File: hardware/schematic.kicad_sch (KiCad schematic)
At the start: 16 parts, among them M1 Arctic_P12_PRO, U1 DS18B20, U2 TC1602A-01T

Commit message: hw: update schematic
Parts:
- removed U2: TC1602A-01T, Display:LCD-016N002L, symbol Display_Character:LCD-016N002L
- added U2: NHD-0420H1Z, Display:NHD-0420H1Z, symbol Display_Character:NHD-0420H1Z
- added U3: PCF8574, symbol Interface_Expansion:PCF8574
- R1: value 220Ω -> 4.7kΩ
- R5: value 15kΩ -> 10kΩ
- R6: value 220Ω -> 2.2kΩ
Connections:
- net +5V: now also U2.2 (VDD), U3.16 (VDD); no longer R6.2
- net GND: now also R6.2, U2.1 (VSS), U2.10 (DB3), U2.16 (K), U2.3 (VO), U2.7 (DB0), U2.8 (DB1), U2.9 (DB2), U3.1 (A0), U3.2 (A1), U3.3 (A2), U3.8 (VSS); no longer R1.2, R3.2
- net at M1.4 (PWM): now also A1.24 (D9); no longer A1.19 (D4)
- net at R4.1, U1.2 (DQ): now also A1.19 (D4); no longer A1.18 (D3)
- net at R6.1: now also R1.2
- net at R1.1: now also R3.2
- net at R3.1, R5.1: now also A1.18 (D3); no longer A1.20 (D5)
- net at A1.31 (SDA/A4): now also U3.15 (SDA)
- net at A1.32 (SCL/A5): now also U3.14 (SCL)
- new net: U2.11 (DB4), U3.9 (P4)
- new net: U2.12 (DB5), U3.10 (P5)
- new net: U2.13 (DB6), U3.11 (P6)
- new net: U2.14 (DB7), U3.12 (P7)
- new net: U2.15 (A), U3.7 (P3)
- new net: U2.4 (RS), U3.4 (P0)
- new net: U2.5 (R/W), U3.5 (P1)
- new net: U2.6 (E), U3.6 (P2)
- no-connect marks 27 -> 23

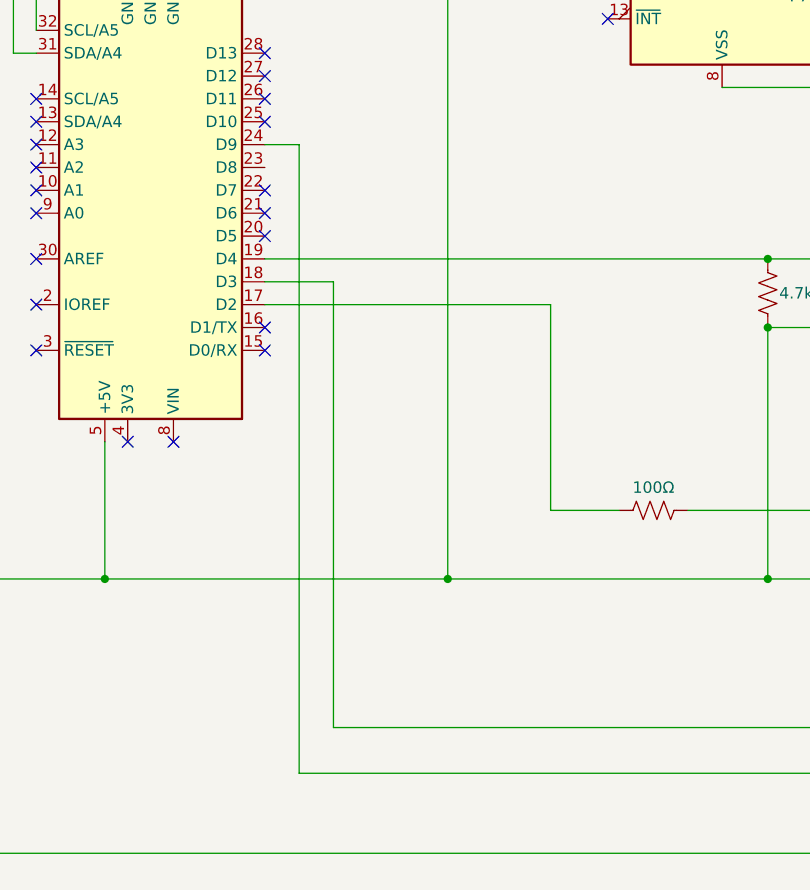
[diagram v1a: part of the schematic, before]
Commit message: hw: update schematic, sw: update pin_definitions.h
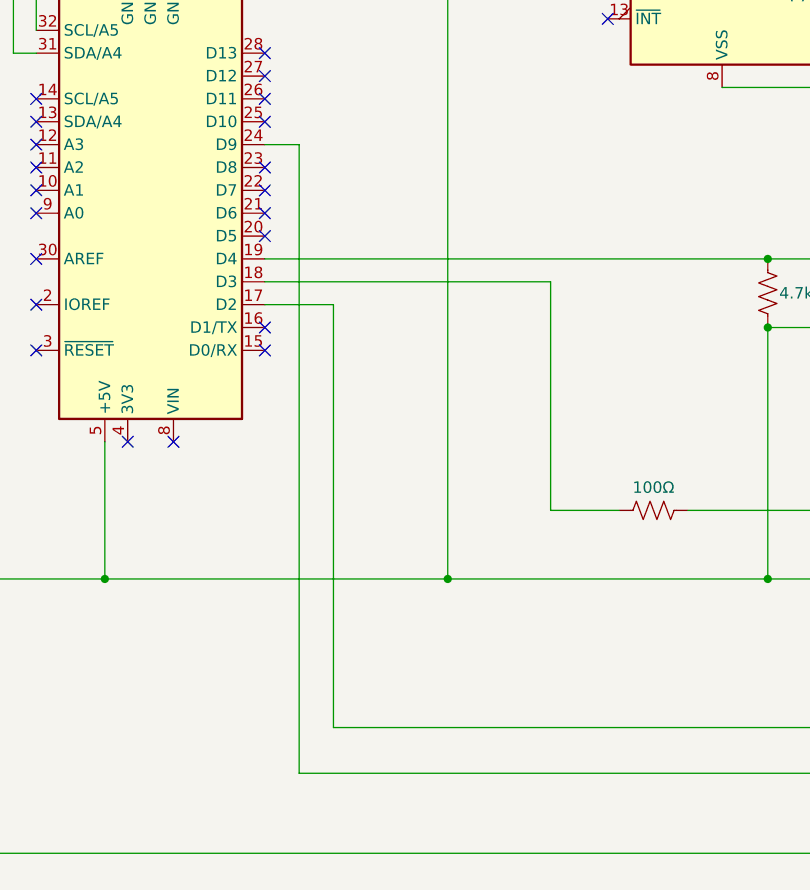
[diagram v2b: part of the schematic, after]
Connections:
- net at R2.1: now also A1.18 (D3); no longer A1.17 (D2)
- net at R3.1, R5.1: now also A1.17 (D2); no longer A1.18 (D3)
- no-connect marks 23 -> 24
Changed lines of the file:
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@@
   (junction (at 45.72 120.65) (diameter 0) (color 0 0 0 0)
   )
+  (no_connect (at 76.2 74.93))
   (no_connect (at 66.04 105.41))
   (no_connect (at 50.8 74.93))
@@
     (stroke (width 0) (type default))
   )
-  (wire (pts (xy 107.95 90.17) (xy 107.95 113.03))
-    (stroke (width 0) (type default))
-  )
   (wire (pts (xy 45.72 44.45) (xy 45.72 120.65))
     (stroke (width 0) (type default))
@@
     (stroke (width 0) (type default))
   )
+  (wire (pts (xy 107.95 113.03) (xy 107.95 87.63))
+    (stroke (width 0) (type default))
+  )
   (wire (pts (xy 109.22 48.26) (xy 109.22 20.32))
     (stroke (width 0) (type default))
@@
     (stroke (width 0) (type default))
   )
+  (wire (pts (xy 83.82 90.17) (xy 76.2 90.17))
+    (stroke (width 0) (type default))
+  )
   (wire (pts (xy 245.11 58.42) (xy 266.7 58.42))
     (stroke (width 0) (type default))
@@
     (stroke (width 0) (type default))
   )
-  (wire (pts (xy 76.2 90.17) (xy 107.95 90.17))
-    (stroke (width 0) (type default))
-  )
   (wire (pts (xy 250.19 142.24) (xy 250.19 144.78))
     (stroke (width 0) (type default))
@@
     (stroke (width 0) (type default))
   )
-  (wire (pts (xy 83.82 87.63) (xy 76.2 87.63))
-    (stroke (width 0) (type default))
-  )
   (wire (pts (xy 267.97 132.08) (xy 250.19 132.08))
     (stroke (width 0) (type default))
@@
     (stroke (width 0) (type default))
   )
+  (wire (pts (xy 107.95 87.63) (xy 76.2 87.63))
+    (stroke (width 0) (type default))
+  )
   (wire (pts (xy 111.76 20.32) (xy 153.67 20.32))
     (stroke (width 0) (type default))
@@
     (stroke (width 0) (type default))
   )
-  (wire (pts (xy 83.82 137.16) (xy 83.82 87.63))
-    (stroke (width 0) (type default))
-  )
   (wire (pts (xy 201.93 55.88) (xy 201.93 68.58))
     (stroke (width 0) (type default))
@@
     (stroke (width 0) (type default))
   )
+  (wire (pts (xy 83.82 137.16) (xy 83.82 90.17))
+    (stroke (width 0) (type default))
+  )

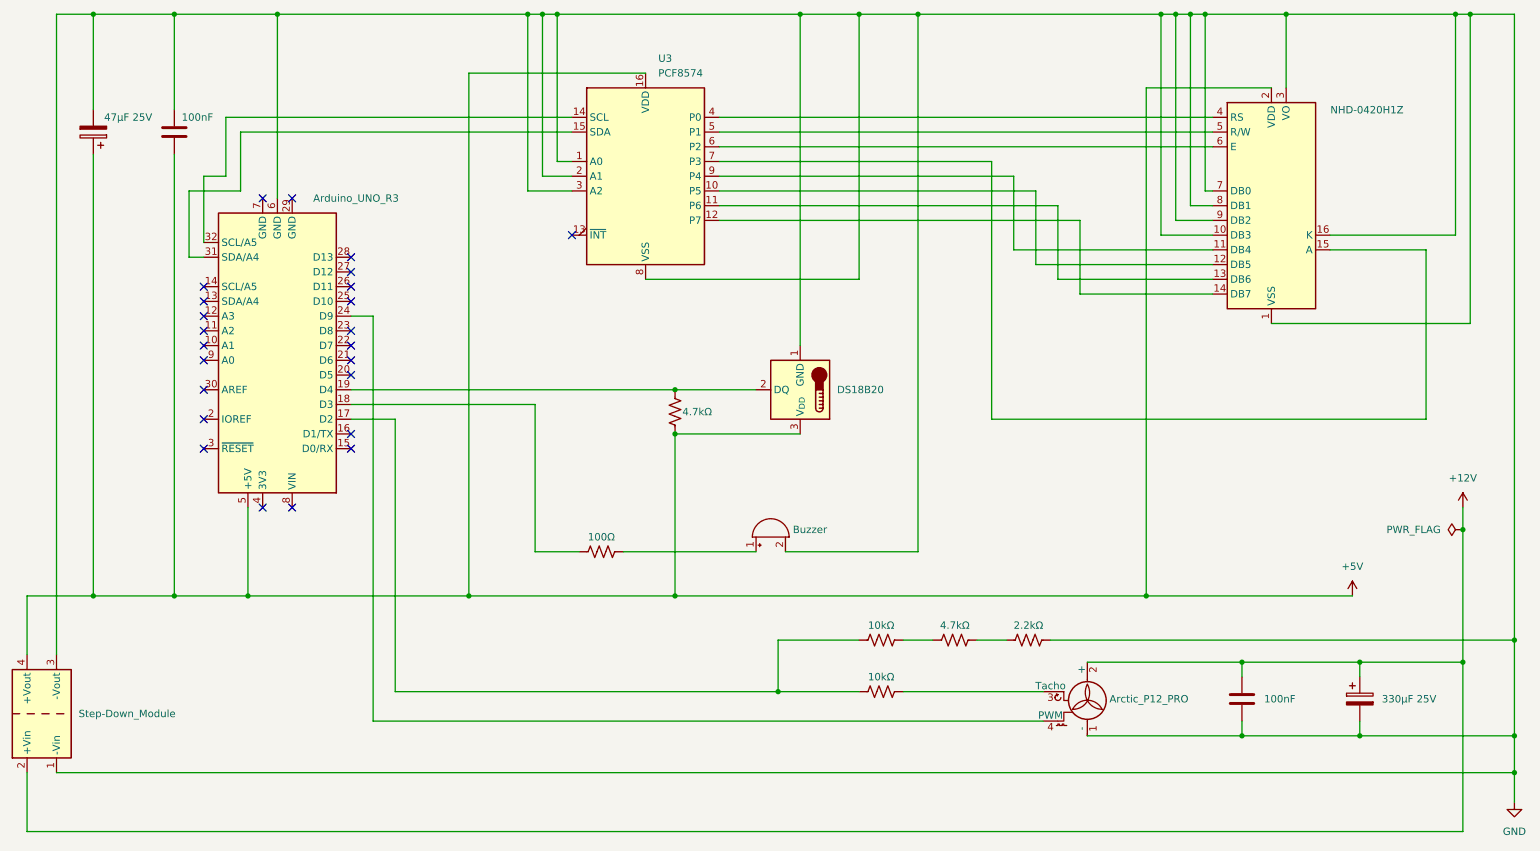
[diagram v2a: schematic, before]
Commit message: add status LEDs to schematic and board configuration
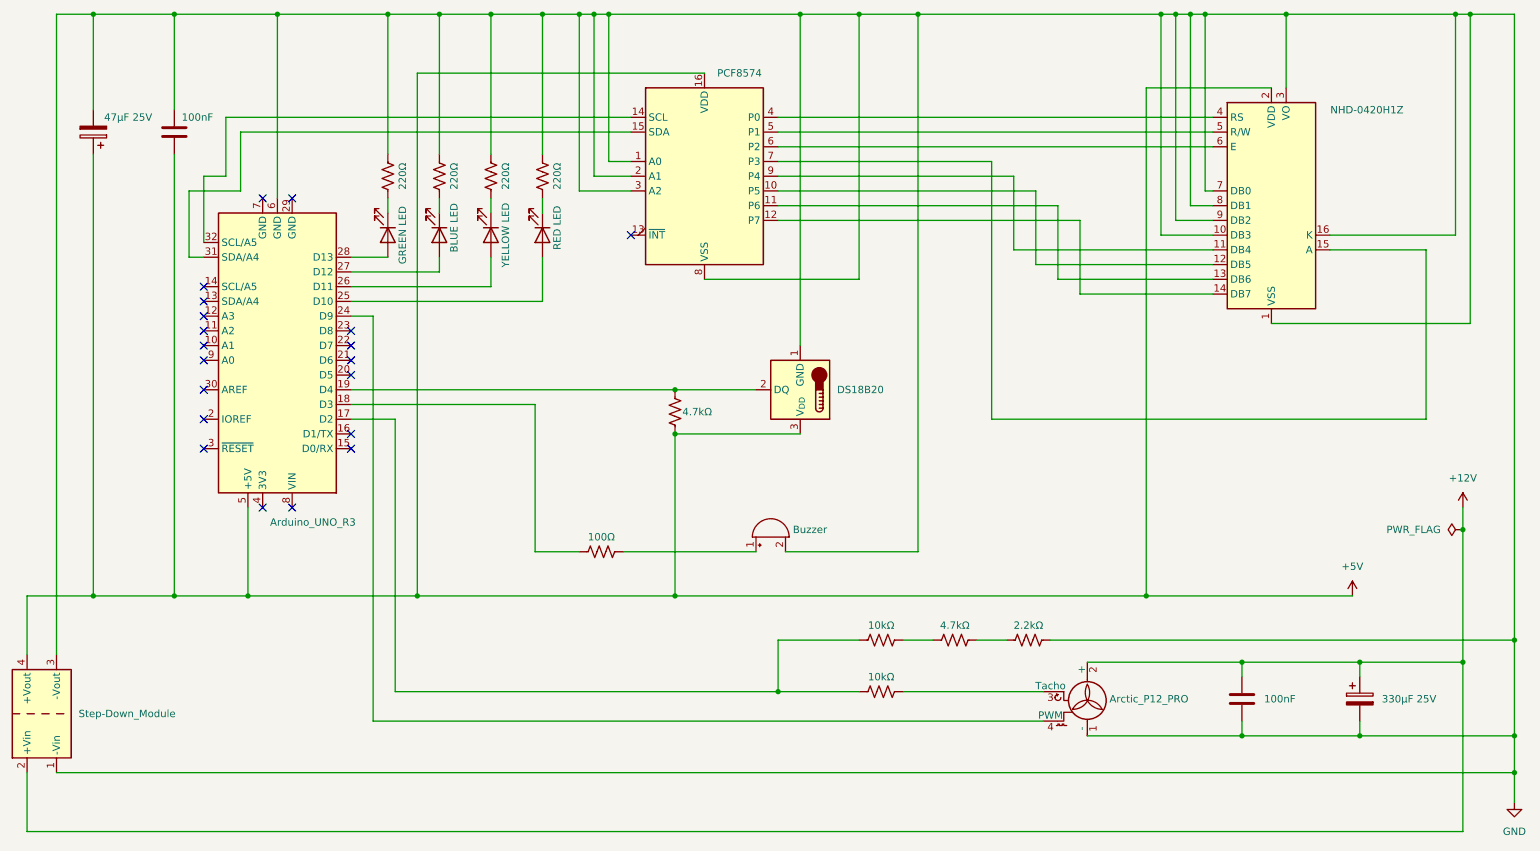
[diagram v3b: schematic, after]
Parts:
- added D1: GREEN LED, symbol Device:LED
- added D2: YELLOW LED, symbol Device:LED
- added D3: BLUE LED, symbol Device:LED
- added D4: RED LED, symbol Device:LED
- added R10, R7, R8, R9: 220Ω, symbol Device:R_US
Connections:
- net GND: now also R10.1, R7.2, R8.2, R9.2
- net at A1.25 (D10): now also D4.2 (A)
- net at A1.26 (D11): now also D2.2 (A)
- net at A1.27 (D12): now also D3.2 (A)
- net at A1.28 (D13): now also D1.2 (A)
- new net: D2.1 (K), R7.1
- new net: D4.1 (K), R8.1
- new net: D1.1 (K), R9.1
- new net: D3.1 (K), R10.2
- no-connect marks 24 -> 20

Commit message: hw: update schematic, sw: update main, config, fan, buzzer, lcd
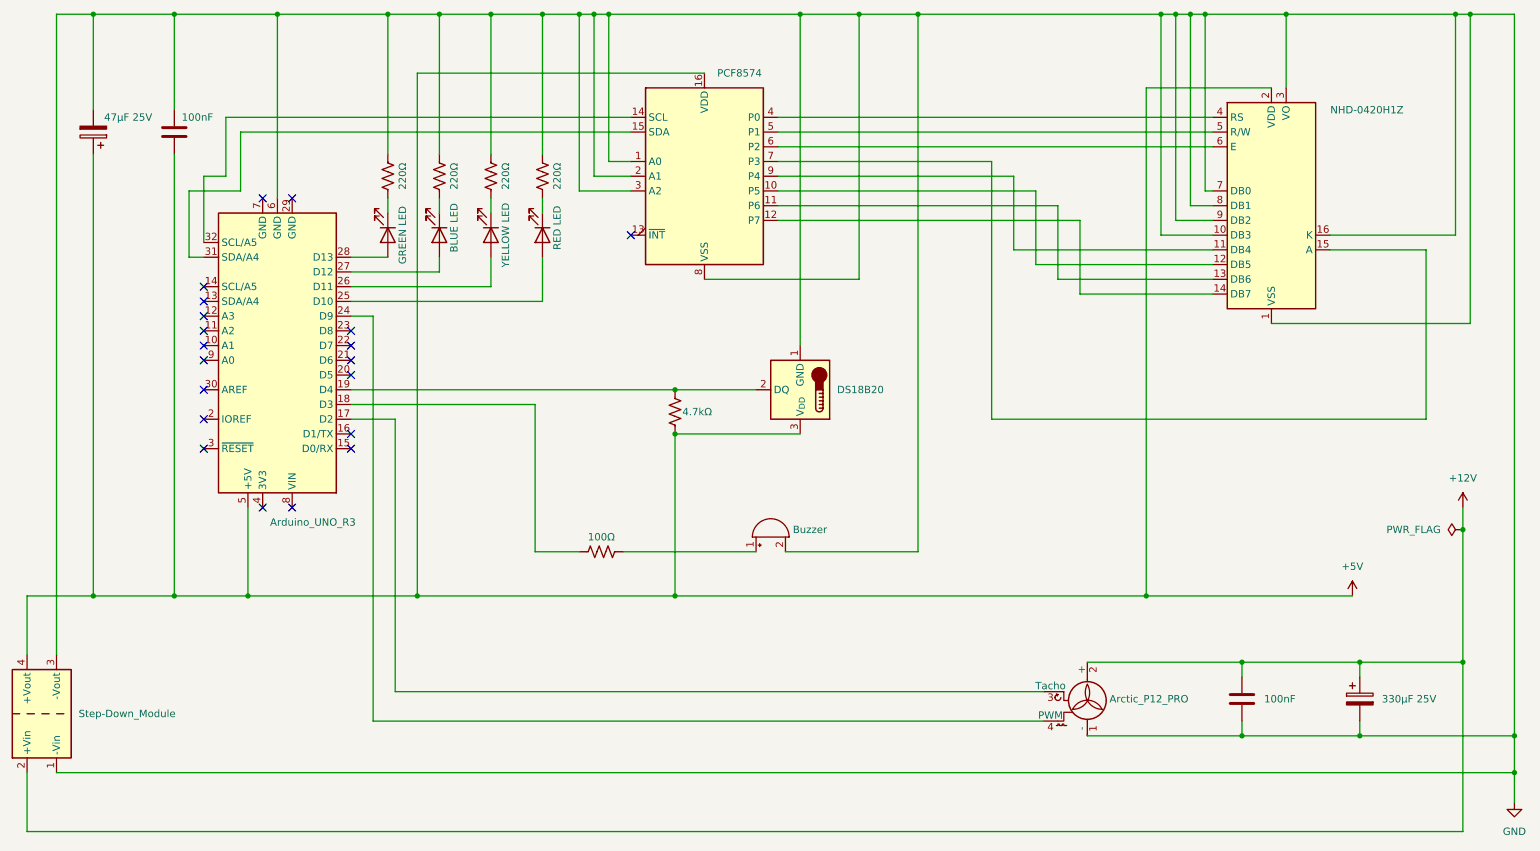
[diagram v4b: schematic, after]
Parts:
- removed R1: 4.7kΩ, symbol Device:R_US
- removed R3, R5: 10kΩ, symbol Device:R_US
- removed R6: 2.2kΩ, symbol Device:R_US
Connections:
- net at M1.3 (Tacho): now also A1.17 (D2)
